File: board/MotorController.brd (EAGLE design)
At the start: 97.8 x 55.9 mm, 39 parts, among them Q1 IPP80P03P4L-04, Q2 8Mhz, T1 BT139X-600E, U1 ATTINY84-20PU

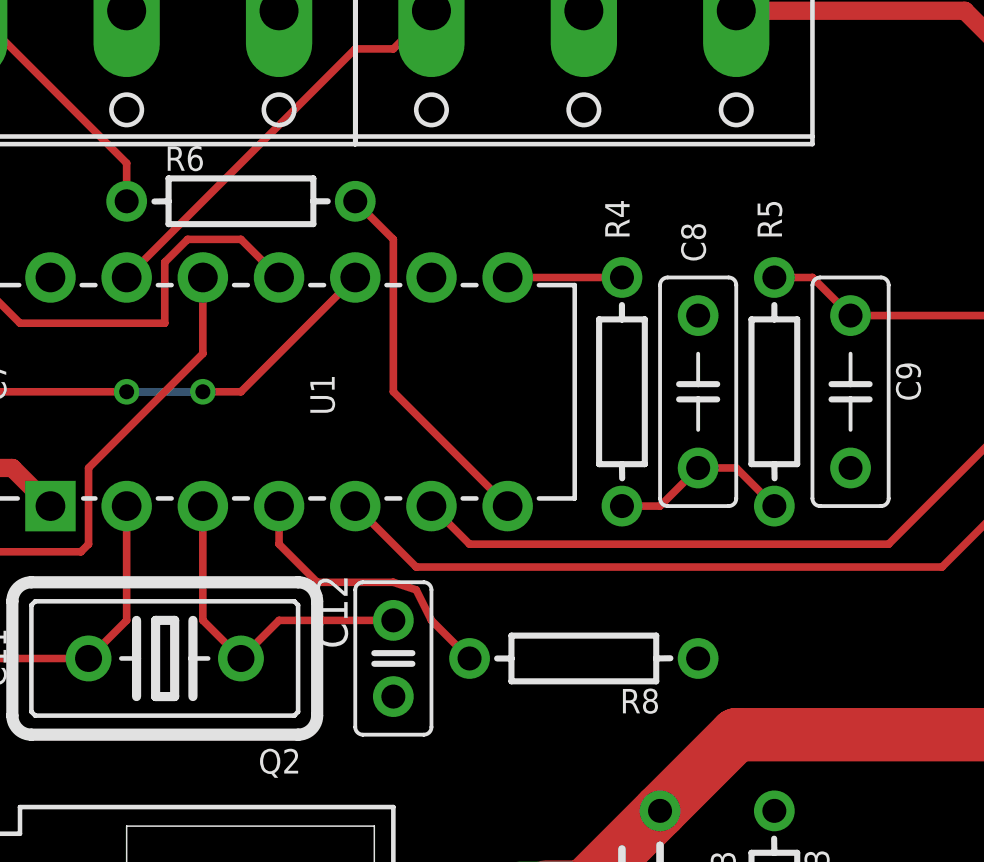
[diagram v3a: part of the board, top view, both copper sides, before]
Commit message: Restore resistor values
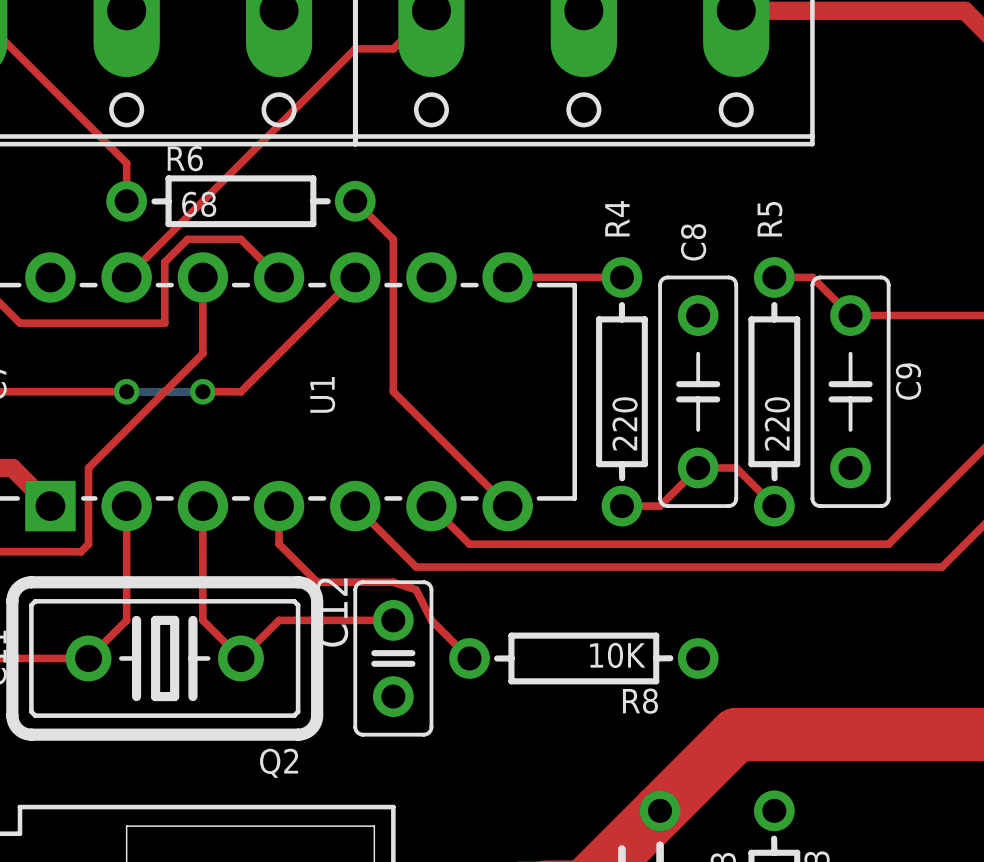
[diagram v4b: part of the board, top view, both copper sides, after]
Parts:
- R1, R2: value (none) -> 1K
- R3, R8: value (none) -> 10K
- R4, R5: value (none) -> 220
- R6: value (none) -> 68
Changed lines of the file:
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@@
 <element name="D2" library="SaintGimp" package="ZDIO-7.5" value="22V" x="63.5" y="10.16" rot="R180"/>
 <element name="D1" library="SaintGimp" package="ZDIO-7.5" value="27V" x="63.5" y="6.35" rot="R180"/>
-<element name="R1" library="SaintGimp" package="AXIAL-7.5MM" value="" x="63.5" y="2.54" rot="R180">
+<element name="R1" library="SaintGimp" package="AXIAL-7.5MM" value="1K" x="63.5" y="2.54" rot="R180">
 <attribute name="VALUE" value="" x="63.5" y="2.54" size="1.778" layer="27" rot="R180" display="off"/>
 </element>
 <element name="C5" library="SaintGimp" package="CAPACITOR-5MM" value="0.1uF" x="64.77" y="17.78" rot="R180"/>
-<element name="R2" library="SaintGimp" package="AXIAL-7.5MM" value="" x="63.5" y="13.97">
+<element name="R2" library="SaintGimp" package="AXIAL-7.5MM" value="1K" x="63.5" y="13.97">
 <attribute name="VALUE" value="" x="63.5" y="13.97" size="1.778" layer="27" display="off"/>
 </element>
 <element name="Q1" library="SaintGimp" package="TO220BH" value="IPP80P03P4L-04" x="29.21" y="16.51" rot="R90"/>
-<element name="R3" library="SaintGimp" package="AXIAL-7.5MM" value="" x="43.18" y="17.78" rot="R270">
+<element name="R3" library="SaintGimp" package="AXIAL-7.5MM" value="10K" x="43.18" y="17.78" rot="R270">
 <attribute name="VALUE" value="" x="43.18" y="17.78" size="1.778" layer="27" rot="R270" display="off"/>
 </element>
@@
 </element>
 <element name="C7" library="SaintGimp" package="CAPACITOR-5MM" value="0.1uF" x="15.24" y="35.56" rot="R270"/>
-<element name="R4" library="SaintGimp" package="AXIAL-7.5MM" value="" x="38.1" y="35.56" smashed="yes" rot="R90">
+<element name="R4" library="SaintGimp" package="AXIAL-7.5MM" value="220" x="38.1" y="35.56" smashed="yes" rot="R90">
 <attribute name="VALUE" value="" x="38.1" y="35.56" size="1.778" layer="27" rot="R90" display="off"/>
 <attribute name="NAME" x="38.354" y="40.64" size="0.8128" layer="25" rot="R90"/>
 <attribute name="VALUE" x="38.608" y="33.528" size="0.8128" layer="21" ratio="10" rot="R90"/>
 </element>
-<element name="R5" library="SaintGimp" package="AXIAL-7.5MM" value="" x="43.18" y="35.56" smashed="yes" rot="R90">
+<element name="R5" library="SaintGimp" package="AXIAL-7.5MM" value="220" x="43.18" y="35.56" smashed="yes" rot="R90">
 <attribute name="VALUE" value="" x="43.18" y="35.56" size="1.778" layer="27" rot="R90" display="off"/>
 <attribute name="NAME" x="43.434" y="40.64" size="0.8128" layer="25" rot="R90"/>
@@
 </element>
 <element name="DC1" library="SaintGimp" package="DC-CONV" value="OKI-78SR-5/1.5-W36H-C" x="67.31" y="45.72"/>
-<element name="R8" library="SaintGimp" package="AXIAL-7.5MM" value="" x="36.83" y="26.67" rot="R180"/>
+<element name="R8" library="SaintGimp" package="AXIAL-7.5MM" value="10K" x="36.83" y="26.67" rot="R180"/>
 <element name="C10" library="SaintGimp" package="CAPACITOR-5MM" value="0.1uF" x="78.74" y="34.29" rot="R270"/>
-<element name="R6" library="SaintGimp" package="AXIAL-7.5MM" value="" x="25.4" y="41.91"/>
+<element name="R6" library="SaintGimp" package="AXIAL-7.5MM" value="68" x="25.4" y="41.91"/>
 <element name="SPD" library="SaintGimp" package="SCREW-TERM-3" value="SCREW-TERM-3" x="36.83" y="48.26" rot="R180"/>
 <element name="MOTOR" library="SaintGimp" package="SCREW-TERM-3" value="SCREW-TERM-3" x="90.17" y="38.1" rot="R90"/>
